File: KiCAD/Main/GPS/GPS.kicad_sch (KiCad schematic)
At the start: 9 parts, among them J8 Conn_Coaxial, U5 MAX-M8Q

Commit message: Replace independent magnetometer, reformat test points, generate test gerber and BOM
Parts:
- TP1, TP3: footprint TestPoint:TestPoint_THTPad_1.5x1.5mm_Drill0.7mm -> TestPoint:TestPoint_Pad_D1.0mm
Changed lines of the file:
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@@
 			)
 		)
-		(property "Footprint" "TestPoint:TestPoint_THTPad_1.5x1.5mm_Drill0.7mm"
+		(property "Footprint" "TestPoint:TestPoint_Pad_D1.0mm"
 			(at 114.3 106.68 0)
 			(effects
@@
 			)
 		)
-		(property "Footprint" "TestPoint:TestPoint_THTPad_1.5x1.5mm_Drill0.7mm"
+		(property "Footprint" "TestPoint:TestPoint_Pad_D1.0mm"
 			(at 109.22 76.2 0)
 			(effects

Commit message: Update BOM and respective components according to LCSC supply, remove previously generated production files
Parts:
- TP1, TP3: now left out of the parts list
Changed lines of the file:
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@@
 		(unit 1)
 		(exclude_from_sim no)
-		(in_bom yes)
+		(in_bom no)
 		(on_board yes)
 		(dnp no)
@@
 		(unit 1)
 		(exclude_from_sim no)
-		(in_bom yes)
-		(on_board yes)
-		(dnp no)
+		(in_bom no)
+		(on_board yes)
+		(dnp no)

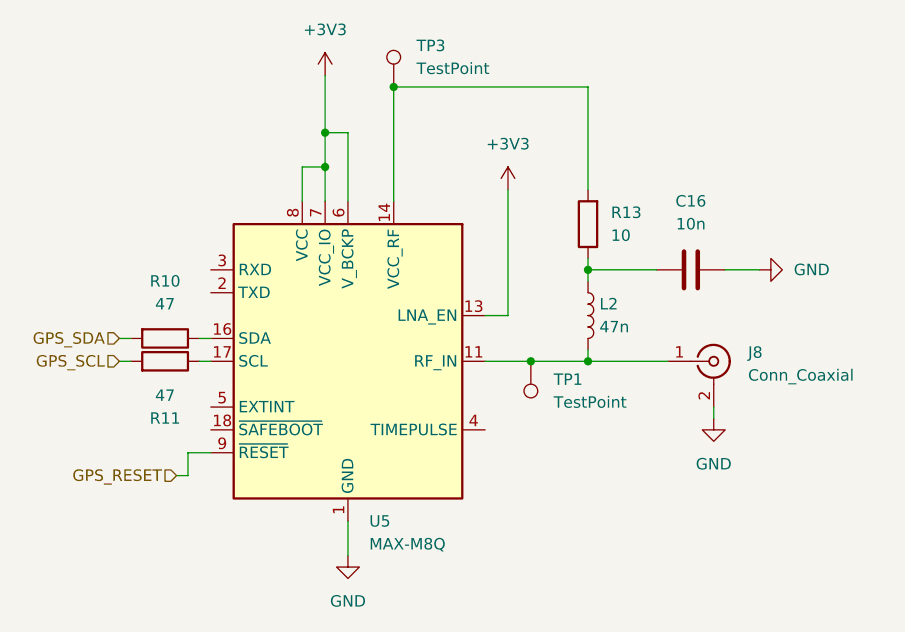
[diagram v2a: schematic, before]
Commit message: save after realizing branch was not switched to layoutv2
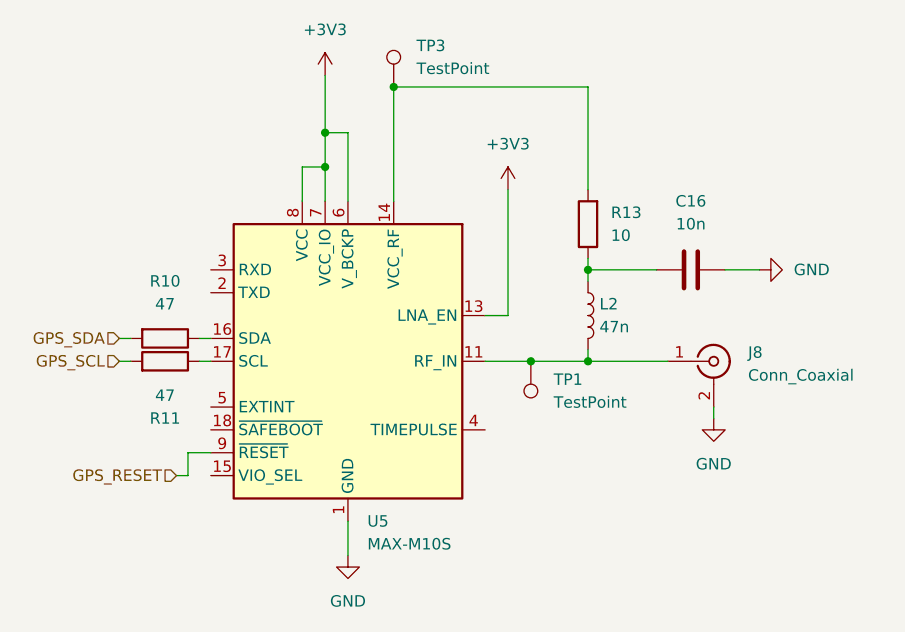
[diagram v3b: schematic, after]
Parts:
- removed U5: MAX-M8Q, RF_GPS:ublox_MAX, symbol RF_GPS:MAX-M8Q
- added U5: MAX-M10S, RF_GPS:ublox_MAX, symbol RF_GPS:MAX-M10S
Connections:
- net +3V3: now also U5.13 (LNA_EN), U5.6 (V_BCKP), U5.7 (VCC_IO), U5.8 (VCC)
- net GND: now also U5.1 (GND), U5.10 (GND), U5.12 (GND)
- net GPS_RESET: now also U5.9 (~{RESET})
- net at J8.1 (In), L2.2, TP1.1: now also U5.11 (RF_IN)
- net at R13.2, TP3.1: now also U5.14 (VCC_RF)
- net at R11.1: now also U5.17 (SCL)
- net at R10.1: now also U5.16 (SDA)
